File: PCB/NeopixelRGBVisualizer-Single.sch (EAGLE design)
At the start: 24 parts, among them CN2 5-12VDC, IC1 MSGEQ7, IC2 78L05ACZ-AP, Q1 16MHz, X1 STEREOJACK

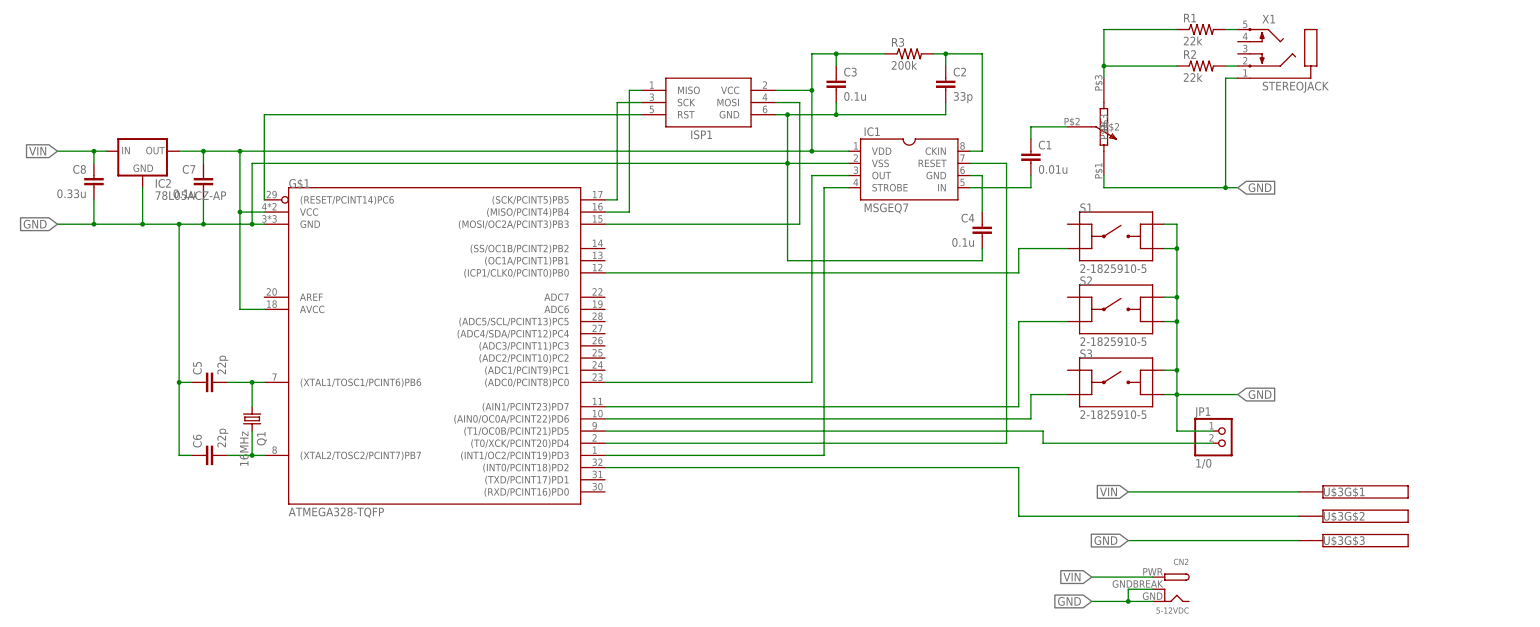
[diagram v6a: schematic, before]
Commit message: Updated board to have correct footprints for tactile switches and potentiometer, since footprints acquired from SnapEDA were wrong.
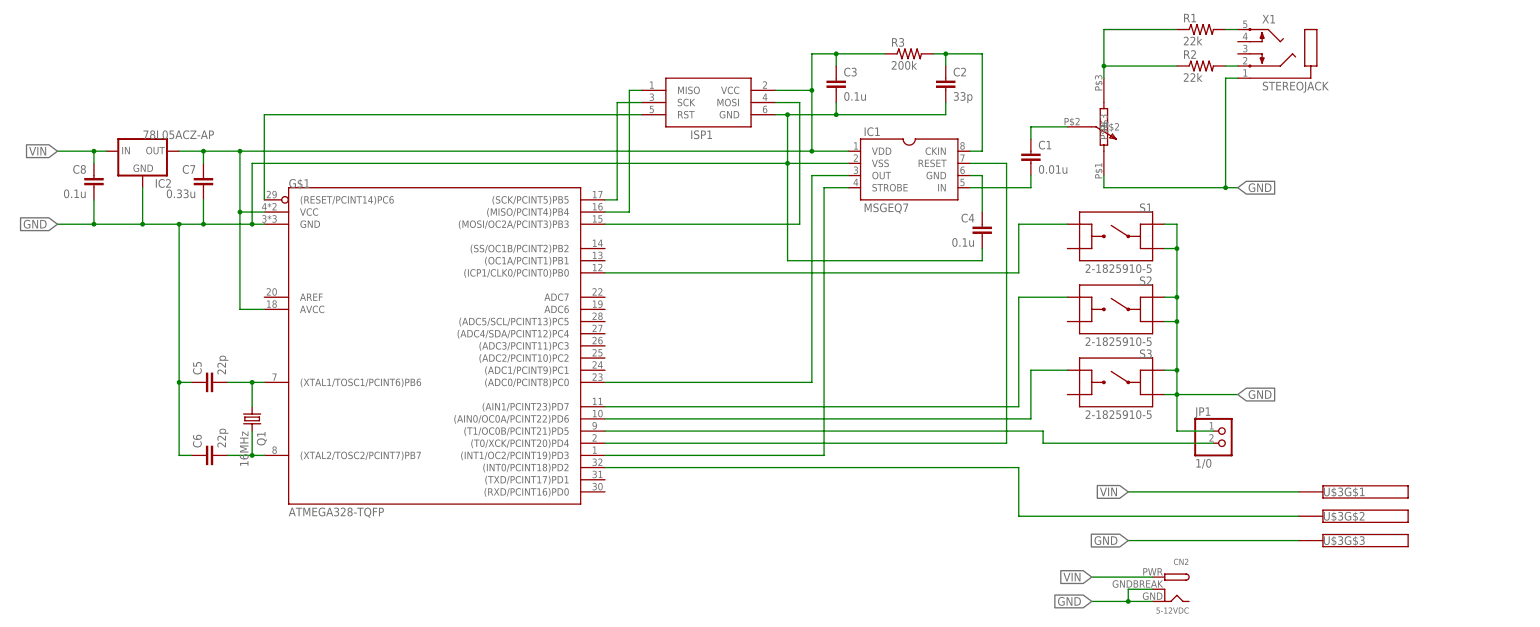
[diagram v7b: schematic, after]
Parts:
- C7: value 0.1u -> 0.33u
- C8: value 0.33u -> 0.1u
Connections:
- net GND: now also S1.1, S2.1, S3.1; no longer S1.4, S2.4, S3.4
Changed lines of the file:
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@@
 <part name="C6" library="rcl" library_urn="urn:adsk.eagle:library:334" deviceset="C-EU" device="C0805" package3d_urn="urn:adsk.eagle:package:23617/2" value="22p"/>
 <part name="CN2" library="adafruit" deviceset="DCBARREL" device="PTH" value="5-12VDC"/>
-<part name="C7" library="rcl" library_urn="urn:adsk.eagle:library:334" deviceset="C-EU" device="C0805" package3d_urn="urn:adsk.eagle:package:23617/2" value="0.1u"/>
-<part name="C8" library="rcl" library_urn="urn:adsk.eagle:library:334" deviceset="C-EU" device="C0805" package3d_urn="urn:adsk.eagle:package:23617/2" value="0.33u"/>
+<part name="C7" library="rcl" library_urn="urn:adsk.eagle:library:334" deviceset="C-EU" device="C0805" package3d_urn="urn:adsk.eagle:package:23617/2" value="0.33u"/>
+<part name="C8" library="rcl" library_urn="urn:adsk.eagle:library:334" deviceset="C-EU" device="C0805" package3d_urn="urn:adsk.eagle:package:23617/2" value="0.1u"/>
 <part name="IC2" library="v-reg" library_urn="urn:adsk.eagle:library:409" deviceset="78LXX" device="" package3d_urn="urn:adsk.eagle:package:30346/1" value="78L05ACZ-AP"/>
 <part name="U$2" library="potentiometers" deviceset="PTD901-2015K" device=""/>
@@
 <instance part="IC2" gate="1" x="-22.86" y="78.74">
 <attribute name="NAME" x="-20.32" y="71.12" size="1.778" layer="95"/>
-<attribute name="VALUE" x="-20.32" y="68.58" size="1.778" layer="96"/>
+<attribute name="VALUE" x="-22.86" y="81.28" size="1.778" layer="96"/>
 </instance>
 <instance part="U$2" gate="G$1" x="177.8" y="83.82" rot="R180"/>
-<instance part="S1" gate="G$1" x="180.34" y="60.96">
-<attribute name="NAME" x="172.719759375" y="66.040159375" size="1.778059375" layer="95"/>
-<attribute name="VALUE" x="172.719540625" y="53.339540625" size="1.778109375" layer="96"/>
-</instance>
-<instance part="S2" gate="G$1" x="180.34" y="45.72">
-<attribute name="NAME" x="172.719759375" y="50.800159375" size="1.778059375" layer="95"/>
-<attribute name="VALUE" x="172.719540625" y="38.099540625" size="1.778109375" layer="96"/>
-</instance>
-<instance part="S3" gate="G$1" x="180.34" y="30.48">
-<attribute name="NAME" x="172.719759375" y="35.560159375" size="1.778059375" layer="95"/>
-<attribute name="VALUE" x="172.719540625" y="22.859540625" size="1.778109375" layer="96"/>
+<instance part="S1" gate="G$1" x="180.34" y="60.96" rot="MR0">
+<attribute name="NAME" x="187.960240625" y="66.040159375" size="1.778059375" layer="95" rot="MR0"/>
+<attribute name="VALUE" x="187.960459375" y="53.339540625" size="1.778109375" layer="96" rot="MR0"/>
+</instance>
+<instance part="S2" gate="G$1" x="180.34" y="45.72" rot="MR0">
+<attribute name="NAME" x="187.960240625" y="50.800159375" size="1.778059375" layer="95" rot="MR0"/>
+<attribute name="VALUE" x="187.960459375" y="38.099540625" size="1.778109375" layer="96" rot="MR0"/>
+</instance>
+<instance part="S3" gate="G$1" x="180.34" y="30.48" rot="MR0">
+<attribute name="NAME" x="187.960240625" y="35.560159375" size="1.778059375" layer="95" rot="MR0"/>
+<attribute name="VALUE" x="187.960459375" y="22.859540625" size="1.778109375" layer="96" rot="MR0"/>
 </instance>
 <instance part="U$3" gate="G$1" x="223.52" y="7.62">
@@
 </segment>
 <segment>
-<pinref part="S3" gate="G$1" pin="4"/>
-<wire x1="190.5" y1="27.94" x2="193.04" y2="27.94" width="0.1524" layer="91"/>
 <wire x1="193.04" y1="27.94" x2="193.04" y2="33.02" width="0.1524" layer="91"/>
-<pinref part="S1" gate="G$1" pin="3"/>
 <wire x1="193.04" y1="33.02" x2="193.04" y2="43.18" width="0.1524" layer="91"/>
 <wire x1="193.04" y1="43.18" x2="193.04" y2="48.26" width="0.1524" layer="91"/>
 <wire x1="193.04" y1="48.26" x2="193.04" y2="58.42" width="0.1524" layer="91"/>
 <wire x1="193.04" y1="58.42" x2="193.04" y2="63.5" width="0.1524" layer="91"/>
-<wire x1="193.04" y1="63.5" x2="190.5" y2="63.5" width="0.1524" layer="91"/>
-<pinref part="S1" gate="G$1" pin="4"/>
-<wire x1="190.5" y1="58.42" x2="193.04" y2="58.42" width="0.1524" layer="91"/>
-<junction x="193.04" y="58.42"/>
-<pinref part="S2" gate="G$1" pin="3"/>
-<wire x1="190.5" y1="48.26" x2="193.04" y2="48.26" width="0.1524" layer="91"/>
-<junction x="193.04" y="48.26"/>
-<pinref part="S2" gate="G$1" pin="4"/>
-<wire x1="190.5" y1="43.18" x2="193.04" y2="43.18" width="0.1524" layer="91"/>
-<junction x="193.04" y="43.18"/>
-<pinref part="S3" gate="G$1" pin="3"/>
-<wire x1="190.5" y1="33.02" x2="193.04" y2="33.02" width="0.1524" layer="91"/>
-<junction x="193.04" y="33.02"/>
 <wire x1="193.04" y1="27.94" x2="205.74" y2="27.94" width="0.1524" layer="91"/>
 <junction x="193.04" y="27.94"/>
@@
 <wire x1="200.66" y1="20.32" x2="193.04" y2="20.32" width="0.1524" layer="91"/>
 <wire x1="193.04" y1="20.32" x2="193.04" y2="27.94" width="0.1524" layer="91"/>
+<pinref part="S1" gate="G$1" pin="1"/>
+<wire x1="190.5" y1="63.5" x2="193.04" y2="63.5" width="0.1524" layer="91"/>
+<pinref part="S2" gate="G$1" pin="1"/>
+<wire x1="190.5" y1="48.26" x2="193.04" y2="48.26" width="0.1524" layer="91"/>
+<junction x="193.04" y="48.26"/>
+<pinref part="S3" gate="G$1" pin="1"/>
+<wire x1="190.5" y1="33.02" x2="193.04" y2="33.02" width="0.1524" layer="91"/>
+<junction x="193.04" y="33.02"/>
+<pinref part="S1" gate="G$1" pin="3"/>
+<wire x1="190.5" y1="58.42" x2="193.04" y2="58.42" width="0.1524" layer="91"/>
+<junction x="193.04" y="58.42"/>
+<pinref part="S2" gate="G$1" pin="3"/>
+<wire x1="190.5" y1="43.18" x2="193.04" y2="43.18" width="0.1524" layer="91"/>
+<junction x="193.04" y="43.18"/>
+<pinref part="S3" gate="G$1" pin="3"/>
+<wire x1="190.5" y1="27.94" x2="193.04" y2="27.94" width="0.1524" layer="91"/>
 </segment>
 </net>
@@
 <net name="N$18" class="0">
 <segment>
-<pinref part="S1" gate="G$1" pin="2"/>
 <pinref part="U$1" gate="G$1" pin="(ICP1/CLK0/PCINT0)PB0"/>
 <wire x1="73.66" y1="53.34" x2="160.02" y2="53.34" width="0.1524" layer="91"/>
-<wire x1="160.02" y1="53.34" x2="160.02" y2="58.42" width="0.1524" layer="91"/>
-<wire x1="160.02" y1="58.42" x2="170.18" y2="58.42" width="0.1524" layer="91"/>
+<pinref part="S1" gate="G$1" pin="2"/>
+<wire x1="160.02" y1="53.34" x2="160.02" y2="63.5" width="0.1524" layer="91"/>
+<wire x1="160.02" y1="63.5" x2="170.18" y2="63.5" width="0.1524" layer="91"/>
 </segment>
 </net>
@@
 <segment>
 <pinref part="U$1" gate="G$1" pin="(AIN0/OC0A/PCINT22)PD6"/>
-<wire x1="170.18" y1="27.94" x2="162.56" y2="27.94" width="0.1524" layer="91"/>
-<wire x1="162.56" y1="27.94" x2="162.56" y2="22.86" width="0.1524" layer="91"/>
 <wire x1="162.56" y1="22.86" x2="73.66" y2="22.86" width="0.1524" layer="91"/>
 <pinref part="S3" gate="G$1" pin="2"/>
+<wire x1="162.56" y1="22.86" x2="162.56" y2="33.02" width="0.1524" layer="91"/>
+<wire x1="162.56" y1="33.02" x2="170.18" y2="33.02" width="0.1524" layer="91"/>
 </segment>
 </net>
@@
 <pinref part="U$1" gate="G$1" pin="(AIN1/PCINT23)PD7"/>
 <wire x1="73.66" y1="25.4" x2="160.02" y2="25.4" width="0.1524" layer="91"/>
-<wire x1="160.02" y1="25.4" x2="160.02" y2="43.18" width="0.1524" layer="91"/>
+<wire x1="160.02" y1="25.4" x2="160.02" y2="48.26" width="0.1524" layer="91"/>
 <pinref part="S2" gate="G$1" pin="2"/>
-<wire x1="160.02" y1="43.18" x2="170.18" y2="43.18" width="0.1524" layer="91"/>
-</segment>
-</net>
+<wire x1="160.02" y1="48.26" x2="170.18" y2="48.26" width="0.1524" layer="91"/>
+</segment>
+</net>

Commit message: Created new branch starting with last good design. proto2 boards did not work for unknown reason.  Tracking reason down now, but, due to time constraints, a new design will be created from the previous known-good branch point.  The new design will fit the project boxes, include 3 tactile switch buttons and one power switch, and use the molex connector from proto2.  It will not include a potentiometer for volume control.  If the problem with the proto2 boards can be determined in the next 2 days, this branch will be scrapped.
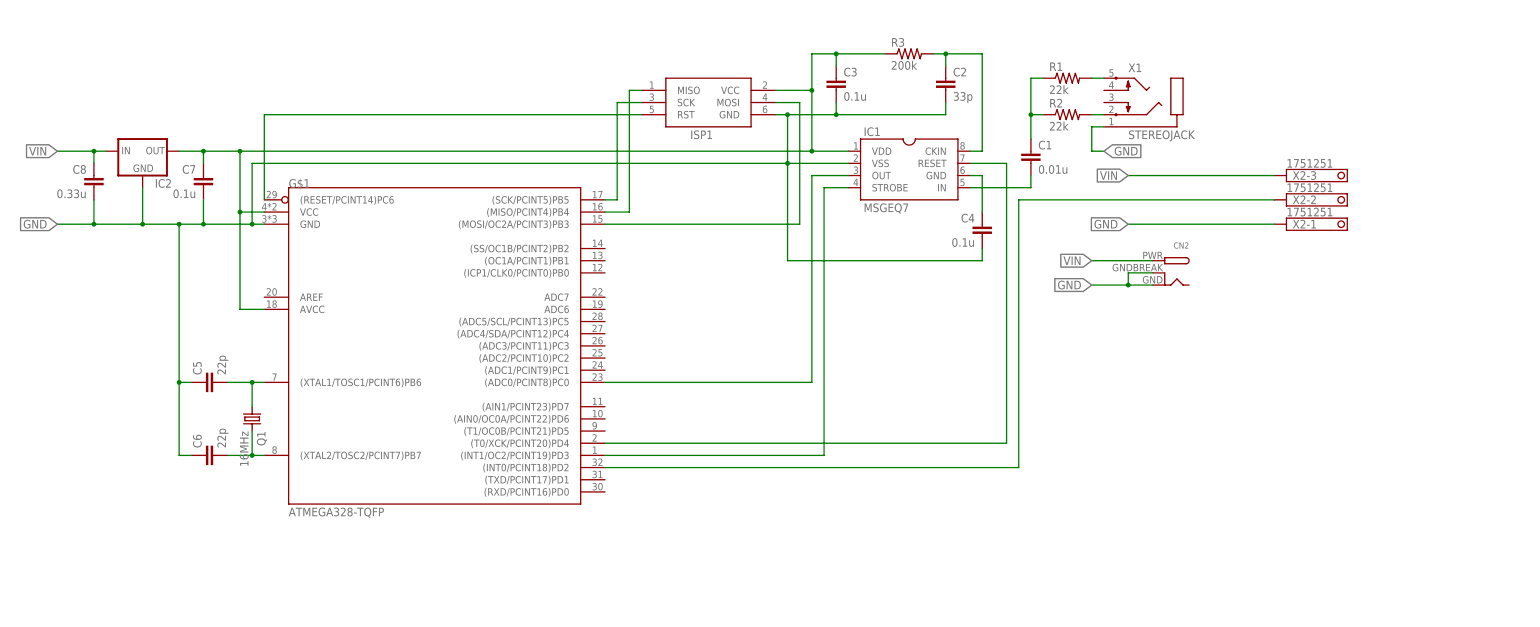
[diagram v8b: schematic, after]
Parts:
- removed JP1: 1/0, mypinhead:PINHD-1X2/ROUND
- removed S1, S2, S3: 2-1825910-5, te_tactileswitch:2-1825910-5
- removed U$2: PTD901-2015K, potentiometers:PTD901-2015K
- removed U$3: 0039303035, MinifitJR:0039303035
- added X2: 1751251, con-phoenix-350:1751251
- C7: value 0.33u -> 0.1u
- C8: value 0.1u -> 0.33u
- CN2: value 5-12VDC -> (none)
- IC2: value 78L05ACZ-AP -> (none)
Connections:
- net MSGEQ7_OUT renamed N$7
- net MSGEQ7_RESET renamed N$9
- net MSGEQ7_STROBE renamed N$8
- removed net N$16: C1.1, U$2.P$2
- removed net N$18: S1.2, U$1.(ICP1/CLK0/PCINT0)PB0
- removed net N$19: S3.2, U$1.(AIN0/OC0A/PCINT22)PD6
- removed net N$20: JP1.2, U$1.(T1/OC0B/PCINT21)PD5
- removed net N$8 (its old number): S2.2, U$1.(AIN1/PCINT23)PD7
- net GND: now also X2-1.K; no longer JP1.1, S1.1, S1.3, S2.1, S2.3, S3.1, S3.3, U$2.P$1, U$3G$3.P$1
- net N$17: now also X2-2.K; no longer U$3G$2.P$1
- net N$6: now also C1.1; no longer U$2.P$3
- net VIN: now also X2-3.K; no longer U$3G$1.P$1
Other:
- moved on the sheet: CN2, R1, R2, X1
